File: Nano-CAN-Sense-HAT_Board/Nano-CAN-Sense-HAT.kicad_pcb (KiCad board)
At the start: 4 copper layers, 46 x 20 mm, 48 parts, among them J1 Analog, J2 Digital, J3 Conn_02x04_Counter_Clockwise, J4 Conn_02x04_Counter_Clockwise, J5 Conn_01x05, J6 Conn_01x03, SW1 SW_Push, SW2 SW_Push, U1 LMC6484, U2 MCP2518FD-xQBB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

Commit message: aestethics, improved lables
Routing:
- net VCC: track 49.7 -> 58.0 mm, vias 1 -> 2
- net +5V: track 37.4 -> 45.7 mm, vias 10 -> 11
- net +3V3: track 7.10 -> 9.17 mm, vias 1 -> 2
- net GND: track 84.1 -> 84.4 mm, vias 20 -> 21
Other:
- board text added: "Sensor to CAN"
- board text added: "github.com/Sarbf1"

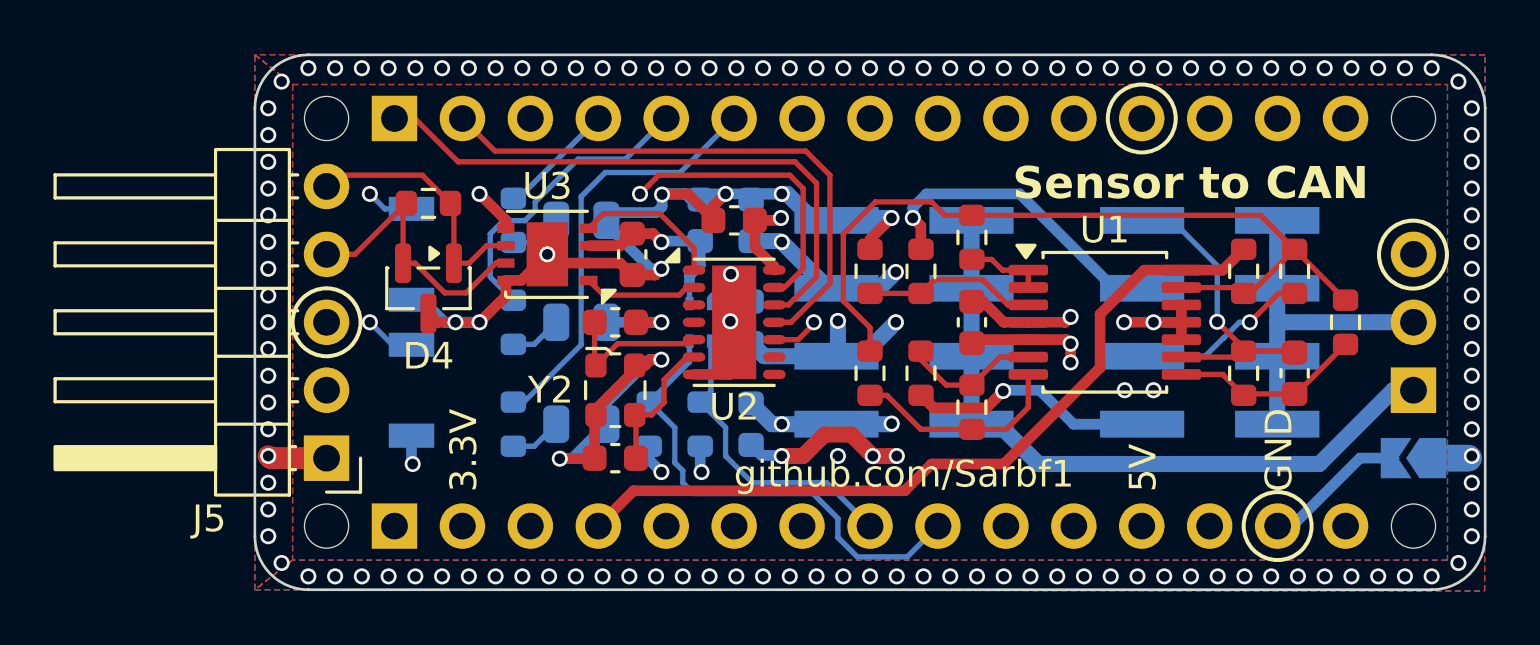
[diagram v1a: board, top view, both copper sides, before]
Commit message: Started draft coding Layout fixes
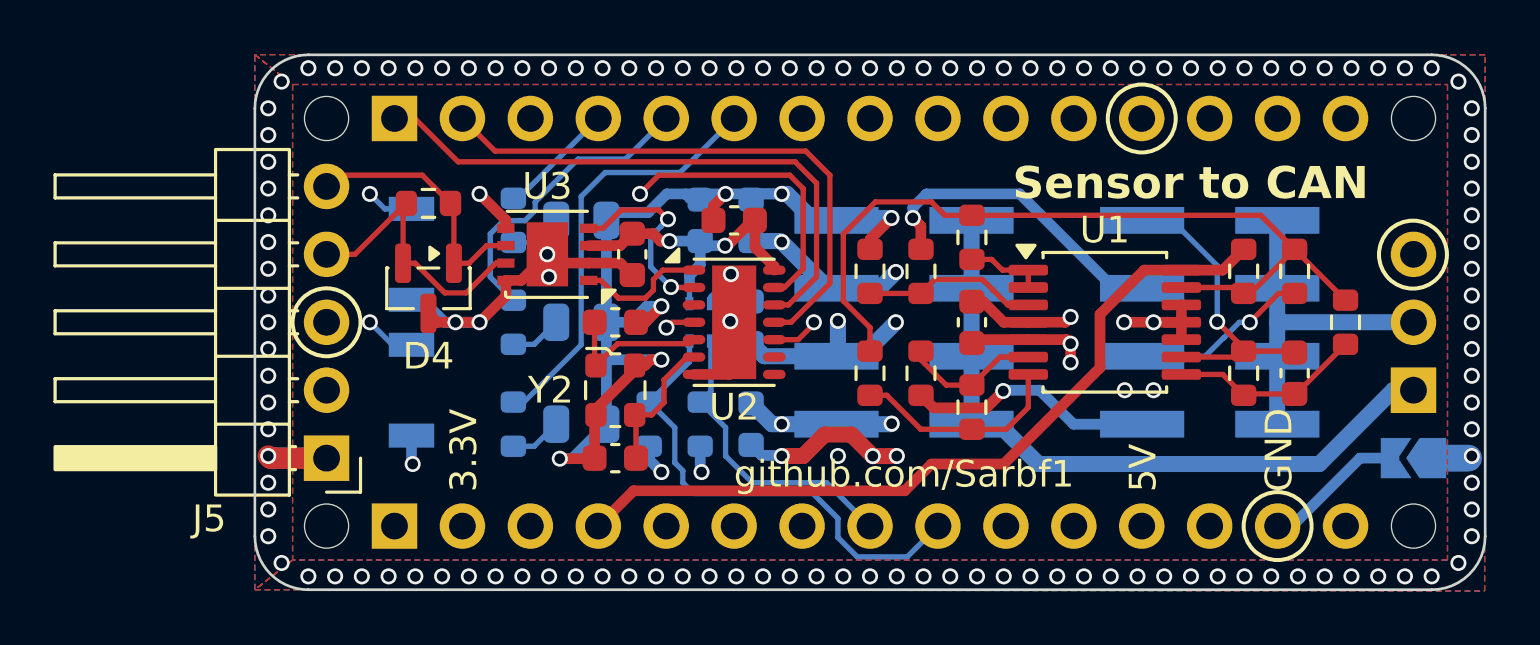
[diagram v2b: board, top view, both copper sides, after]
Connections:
- J2 pad 11: /D2 -> /CANINT
- U2 pad 4: unconnected-(U2-~{INT}-Pad4) -> /CANINT
- U3 pad 1: Net-(U2-RXCAN) -> Net-(U2-TXCAN)
- U3 pad 4: Net-(U2-TXCAN) -> Net-(U2-RXCAN)
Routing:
- net /CANINT: track 0.00 -> 21.9 mm, vias 0 -> 1
- net Net-(U2-RXCAN): track 4.28 -> 7.38 mm, vias 0 -> 2
- net +5V: track 45.7 -> 44.3 mm
- net GND: track 84.4 -> 83.6 mm, vias 21 -> 20
- net Net-(U2-TXCAN): track 5.53 -> 4.88 mm

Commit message: Changed OpAmp, improved lables
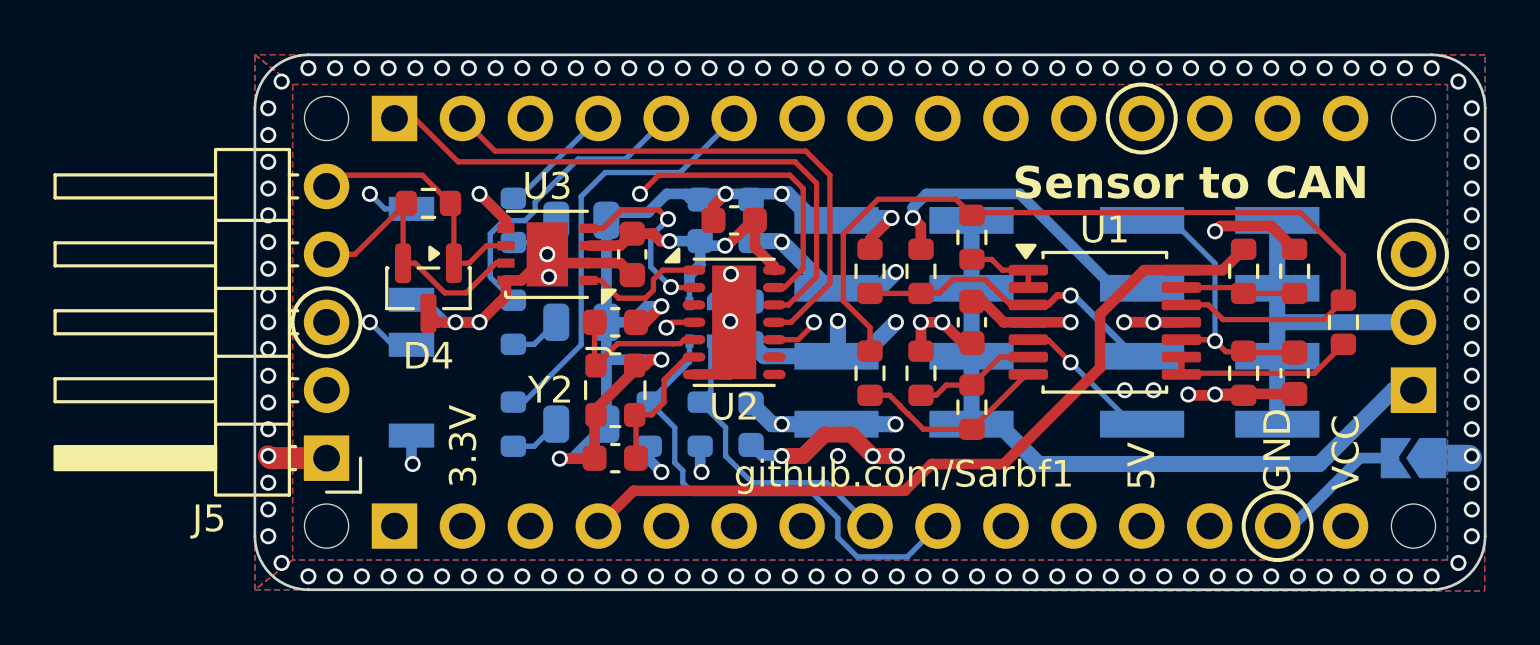
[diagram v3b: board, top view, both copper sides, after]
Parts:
- removed C1: 100nC, Capacitor_SMD:C_0603_1608Metric
- removed R6: 250R, Resistor_SMD:R_0603_1608Metric
- added C11: 100nC, Capacitor_SMD:C_0603_1608Metric, F.Cu at (137.5, 93.0)
- added R17: 250R, Resistor_SMD:R_0603_1608Metric, F.Cu at (135.6, 93.0)
- R12: value 1kR -> 2kR
- R5: value 1.5kR -> 2kR
- R7: value 1k8R -> 2kR
- R8: value 1k3R -> 1kR
- U1: value LMC6484 -> NCS20074DTB
- moved R10 0.08 mm to (139.3, 91.1)
- turned R13 to 90 degrees
- turned R5 to -90 degrees
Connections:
- R10 pad 1: Net-(U1D--) -> Net-(U1D-+)
- R10 pad 2: Net-(C1-Pad1) -> Net-(U1C--)
- R11 pad 1: Net-(U1D--) -> Net-(U1D-+)
- R13 pad 2: /sense5V -> GND
- R5 pad 1: /sense3.3V -> GND
- R7 pad 1: Net-(U1A-+) -> /sense5V
- R8 pad 2: Net-(U1A-+) -> /sense5V
- R9 pad 1: Net-(U1D--) -> Net-(U1D-+)
- U1 pad 10: GND -> /sense_Current
- U1 pad 12: GND -> Net-(U1D-+)
- U1 pad 3: Net-(U1A-+) -> /sense5V
- U1 pad 5: GND -> /sense3.3V
- U1 pad 8: Net-(C1-Pad1) -> Net-(U1C--)
- U1 pad 9: /sense_Current -> Net-(U1C--)
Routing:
- net Net-(U1D-+): track 0.00 -> 33.2 mm
- net Net-(U1D--): track 30.6 -> 4.32 mm
- net Net-(C1-Pad1): track 7.25 -> 0.00 mm
- net Net-(U1C--): track 0.00 -> 7.17 mm
- net Net-(U1A-+): track 6.53 -> 0.00 mm
- net GND: track 83.6 -> 90.1 mm, vias 20 -> 23
- net /sense5V: track 7.03 -> 11.9 mm
- net /sense3.3V: track 9.26 -> 5.57 mm
- net Net-(R11-Pad2): track 8.01 -> 7.31 mm
- net Net-(U1B--): track 5.16 -> 4.60 mm
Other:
- board text added: "VCC"

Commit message: Opamp supply 12V, Added Zener for protection
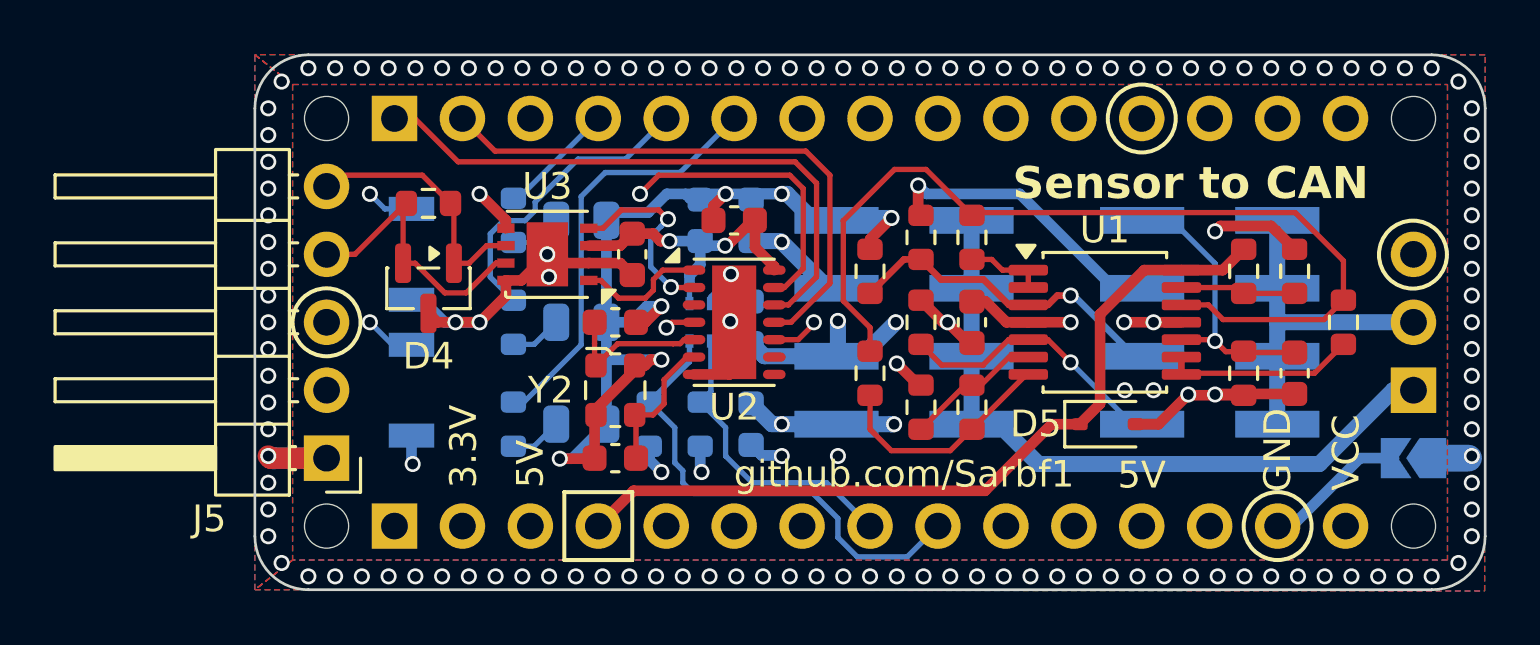
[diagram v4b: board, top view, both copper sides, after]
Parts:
- added D5: D_Zener_5.1V, Diode_SMD:D_SOD-323, F.Cu at (130.5, 94.9)
- added R18: 1kR, Resistor_SMD:R_0603_1608Metric, F.Cu at (123.5, 91.1)
- moved R5 1.27 mm to (123.5, 94.3)
- moved R7 1.27 mm to (123.5, 87.9)
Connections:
- C6 pad 1: +5V -> VCC
- U1 pad 4: +5V -> VCC
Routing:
- net /sense3.3V: track 5.57 -> 10.3 mm
- net +5V: track 44.2 -> 40.1 mm, vias 11 -> 10
- net GND: track 90.1 -> 87.8 mm, vias 23 -> 21
- net Net-(R11-Pad2): track 7.31 -> 8.71 mm
- net Net-(U1D-+): track 33.2 -> 34.3 mm
- net /sense12V: track 11.9 -> 11.1 mm
- net /A0: track 29.6 -> 30.4 mm
- net /sense5V: track 11.9 -> 12.5 mm
- net VCC: track 58.0 -> 58.5 mm
- net Net-(U1B--): track 4.60 -> 5.13 mm

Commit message: Improved lables, better 5V protection diode, new images
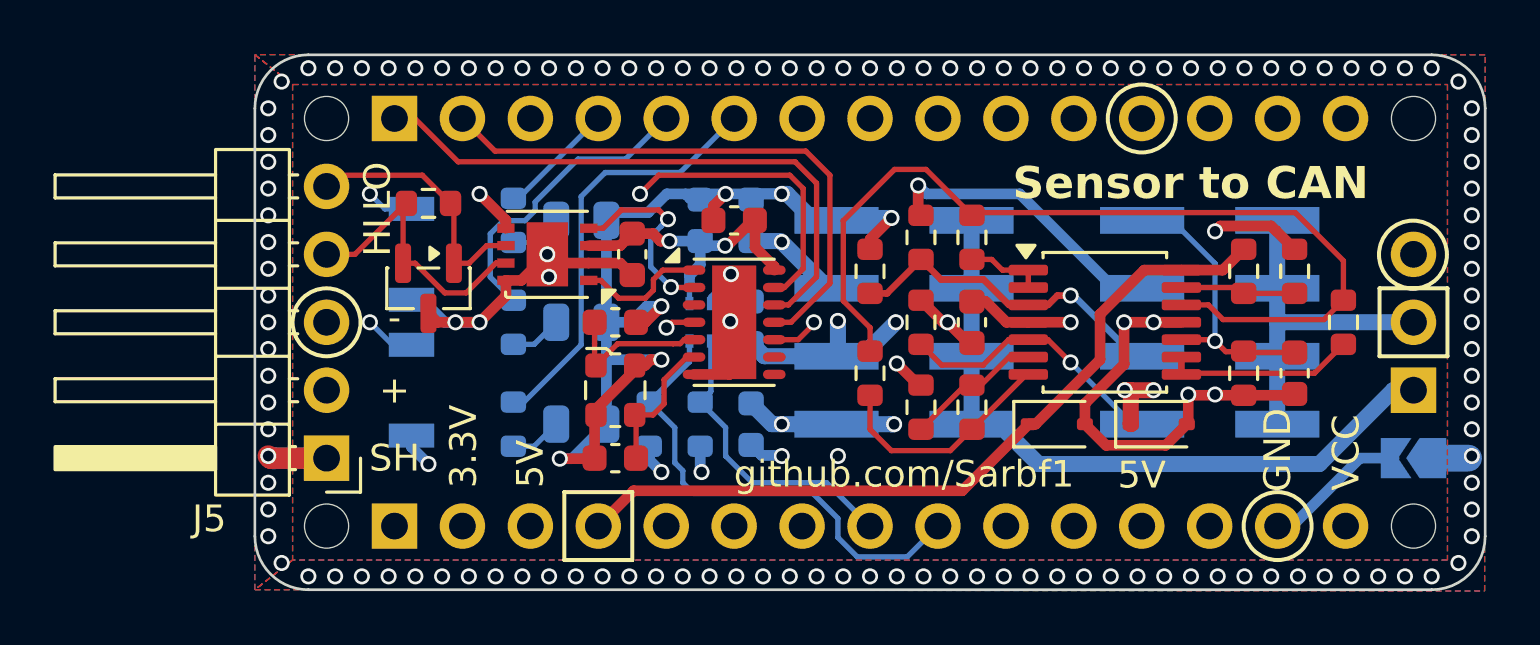
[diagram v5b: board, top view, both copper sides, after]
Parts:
- added D6: D_Zener_5.1V, Diode_SMD:D_SOD-323, F.Cu at (132.4, 94.9)
- moved D5 1.91 mm to (128.6, 94.9)
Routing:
- net GND: track 87.8 -> 94.5 mm
- net +5V: track 40.1 -> 42.7 mm
- net /A0: track 30.4 -> 29.4 mm
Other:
- board text added: "+"
- board text added: "-"
- board text added: "HI"
- board text added: "LO"
- board text added: "SH"
